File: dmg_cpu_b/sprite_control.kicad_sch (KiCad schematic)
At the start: 138 parts

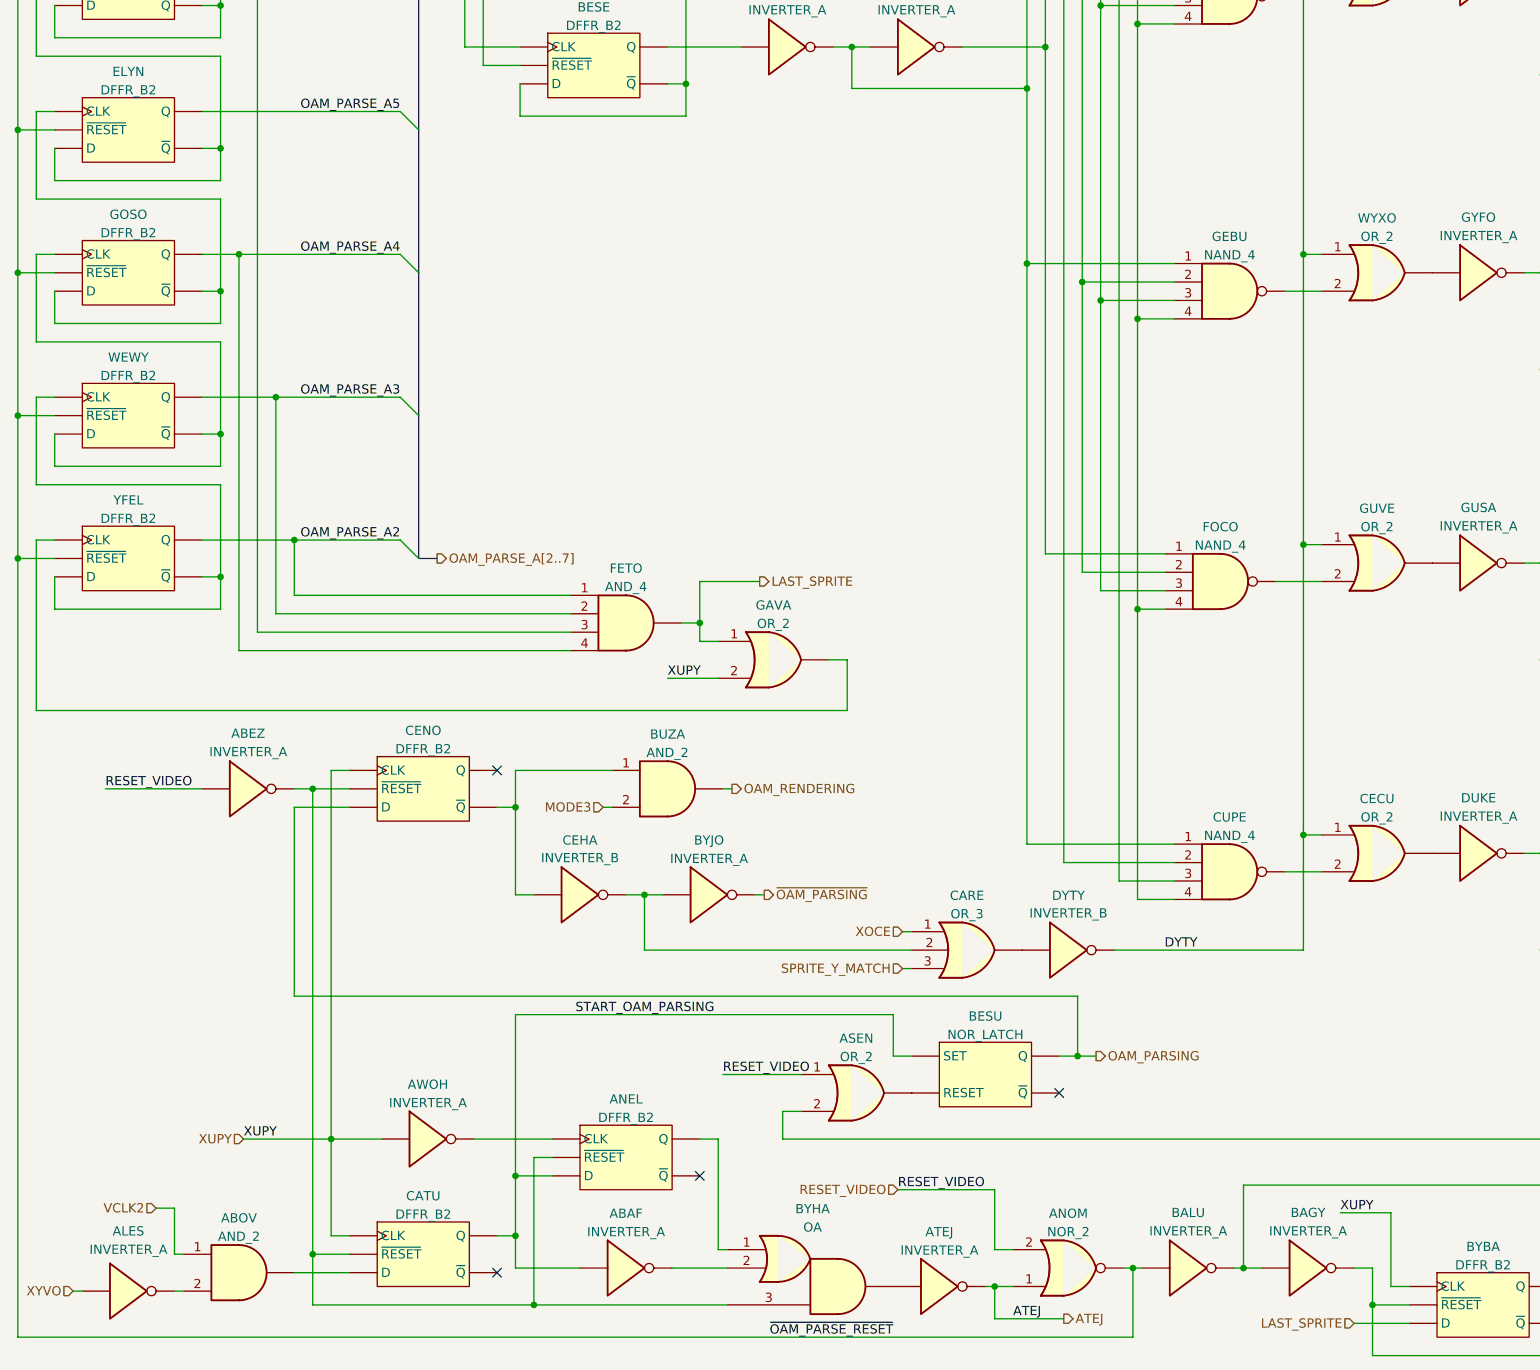
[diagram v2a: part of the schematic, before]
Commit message: Changes made based on review. PPU hierarchcal sheet work started.
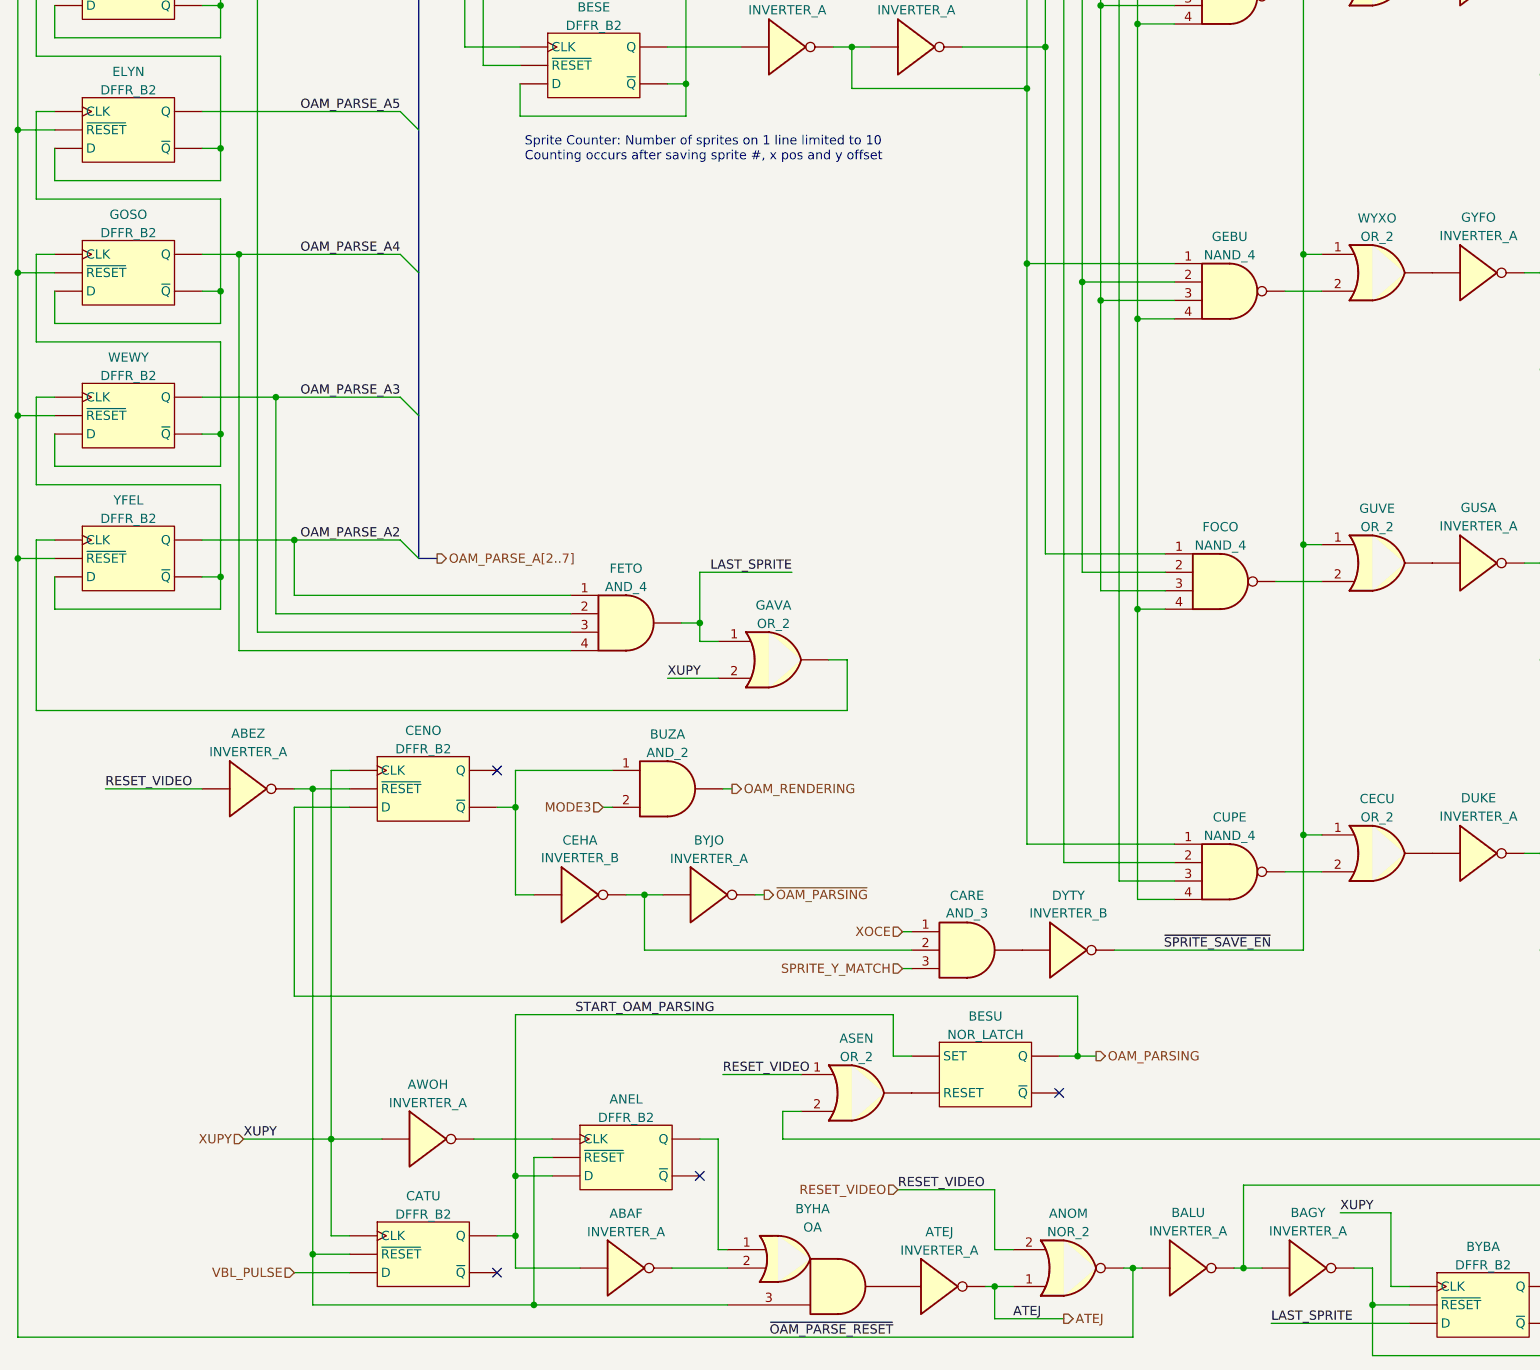
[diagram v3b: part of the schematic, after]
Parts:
- removed ABOV: AND_2, symbol DMG_CPU_Cells:AND_2
- removed ALES: INVERTER_A, symbol DMG_CPU_Cells:INVERTER_A
- CARE: value OR_3 -> AND_3; symbol DMG_CPU_Cells:OR_3 -> DMG_CPU_Cells:AND_3
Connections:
- net VBL_PULSE: now reaches CATU.3 (D)
- net DYTY renamed ~{SPRITE_SAVE_EN}
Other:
- note added: "Sprite Counter: Number of sprites on 1 line limited to 10 Counting occurs after saving sprite #, x pos and y offset"
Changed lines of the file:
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@@
     (stroke (width 0) (type default) (color 0 0 0 0))
   )
-  (wire (pts (xy 24.13 273.685) (xy 25.4 273.685))
-    (stroke (width 0) (type default) (color 0 0 0 0))
-  )
   (wire (pts (xy 46.99 130.81) (xy 46.99 185.42))
     (stroke (width 0) (type default) (color 0 0 0 0))
@@
     (stroke (width 0) (type default) (color 0 0 0 0))
   )
-  (wire (pts (xy 110.49 175.895) (xy 118.745 175.895))
+  (wire (pts (xy 110.49 174.625) (xy 123.19 174.625))
     (stroke (width 0) (type default) (color 0 0 0 0))
   )
@@
     (stroke (width 0) (type default) (color 0 0 0 0))
   )
-  (wire (pts (xy 38.1 262.255) (xy 38.1 268.605))
-    (stroke (width 0) (type default) (color 0 0 0 0))
-  )
   (bus (pts (xy 279.4 135.89) (xy 279.4 95.25))
     (stroke (width 0) (type default) (color 0 0 0 0))
@@
     (stroke (width 0) (type default) (color 0 0 0 0))
   )
-  (wire (pts (xy 110.49 181.61) (xy 110.49 175.895))
+  (wire (pts (xy 110.49 181.61) (xy 110.49 174.625))
     (stroke (width 0) (type default) (color 0 0 0 0))
   )
@@
     (stroke (width 0) (type default) (color 0 0 0 0))
   )
-  (wire (pts (xy 38.1 268.605) (xy 39.37 268.605))
-    (stroke (width 0) (type default) (color 0 0 0 0))
-  )
   (wire (pts (xy 155.575 51.435) (xy 175.895 51.435))
     (stroke (width 0) (type default) (color 0 0 0 0))
@@
     (stroke (width 0) (type default) (color 0 0 0 0))
   )
-  (wire (pts (xy 38.1 273.685) (xy 39.37 273.685))
-    (stroke (width 0) (type default) (color 0 0 0 0))
-  )
   (wire (pts (xy 302.26 51.435) (xy 284.48 51.435))
     (stroke (width 0) (type default) (color 0 0 0 0))
@@
     (stroke (width 0) (type default) (color 0 0 0 0))
   )
-  (wire (pts (xy 200.66 278.13) (xy 208.28 278.13))
+  (wire (pts (xy 189.23 278.13) (xy 208.28 278.13))
     (stroke (width 0) (type default) (color 0 0 0 0))
   )
@@
     (stroke (width 0) (type default) (color 0 0 0 0))
   )
-  (wire (pts (xy 35.56 262.255) (xy 38.1 262.255))
-    (stroke (width 0) (type default) (color 0 0 0 0))
-  )
   (wire (pts (xy 160.655 53.975) (xy 175.895 53.975))
     (stroke (width 0) (type default) (color 0 0 0 0))
@@
     (stroke (width 0) (type default) (color 0 0 0 0))
   )
+  (text "Sprite Counter: Number of sprites on 1 line limited to 10\nCounting occurs after saving sprite #, x pos and y offset"
+    (at 86.36 118.11 0)
+    (effects (font (size 1.27 1.27)) (justify left bottom))
+  )
   (label "SAVE_SPRITE_NUM_0" (at 269.24 66.04 180)
     (effects (font (size 1.27 1.27)) (justify right bottom))
@@
     (effects (font (size 1.27 1.27)) (justify right bottom))
   )
+  (label "LAST_SPRITE" (at 189.23 278.13 0)
+    (effects (font (size 1.27 1.27)) (justify left bottom))
+  )
   (label "SAVE_SPRITE_X_0" (at 269.24 52.705 180)
     (effects (font (size 1.27 1.27)) (justify right bottom))
@@
     (effects (font (size 1.27 1.27)) (justify right bottom))
   )
+  (label "LAST_SPRITE" (at 123.19 174.625 180)
+    (effects (font (size 1.27 1.27)) (justify right bottom))
+  )
   (label "SAVE_SPRITE_NUM_3" (at 269.24 186.69 180)
     (effects (font (size 1.27 1.27)) (justify right bottom))
@@
     (effects (font (size 1.27 1.27)) (justify right bottom))
   )
-  (label "DYTY" (at 179.07 226.695 180)
+  (label "~{SPRITE_SAVE_EN}" (at 189.23 226.695 180)
     (effects (font (size 1.27 1.27)) (justify right bottom))
   )
@@
     (effects (font (size 1.27 1.27)) (justify right bottom))
   )
-  (hierarchical_label "LAST_SPRITE" (shape output) (at 118.745 175.895 0)
-    (effects (font (size 1.27 1.27)) (justify left))
-  )
-  (hierarchical_label "RESET_VIDEO" (shape input) (at 137.795 259.715 180)
+  (hierarchical_label "VBL_PULSE" (shape input) (at 54.61 271.145 180)
     (effects (font (size 1.27 1.27)) (justify right))
   )
-  (hierarchical_label "VCLK2" (shape input) (at 35.56 262.255 180)
+  (hierarchical_label "RESET_VIDEO" (shape input) (at 137.795 259.715 180)
     (effects (font (size 1.27 1.27)) (justify right))
   )
@@
     (effects (font (size 1.27 1.27)) (justify left))
   )
-  (hierarchical_label "XYVO" (shape input) (at 24.13 273.685 180)
-    (effects (font (size 1.27 1.27)) (justify right))
-  )
   (hierarchical_label "OAM_PARSE_A[2..7]" (shape output) (at 74.295 172.72 0)
     (effects (font (size 1.27 1.27)) (justify left))
   )
-  (hierarchical_label "LAST_SPRITE" (shape input) (at 200.66 278.13 180)
-    (effects (font (size 1.27 1.27)) (justify right))
-  )
   (hierarchical_label "MODE3" (shape input) (at 97.155 207.01 180)
     (effects (font (size 1.27 1.27)) (justify right))
@@
     (pin "3")
   )
-  (symbol (lib_id "DMG_CPU_Cells:OR_3") (at 147.32 226.695 0) (unit 1)
-    (in_bom yes) (on_board yes) (fields_autoplaced)
+  (symbol (lib_id "DMG_CPU_Cells:AND_3") (at 147.32 226.695 0) (unit 1)
+    (in_bom yes) (on_board yes)
     (property "Reference" "CARE" (id 0) (at 147.3198 219.1852 0))
-    (property "Value" "OR_3" (id 1) (at 147.3198 221.7221 0))
-    (property "Footprint" "" (id 2) (at 147.066 226.695 0)
+    (property "Value" "AND_3" (id 1) (at 147.32 221.615 0))
+    (property "Footprint" "" (id 2) (at 147.32 226.695 0)
       (effects (font (size 1.27 1.27)) hide)
     )
-    (property "Datasheet" "http://iceboy.a-singer.de/doc/dmg_cells.html#or3" (id 3) (at 147.32 234.315 0)
+    (property "Datasheet" "http://iceboy.a-singer.de/doc/dmg_cells.html#and3" (id 3) (at 147.32 234.315 0)
       (effects (font (size 1.27 1.27)) hide)
     )
@@
     (pin "6")
   )
-  (symbol (lib_id "DMG_CPU_Cells:INVERTER_A") (at 31.75 273.685 0) (unit 1)
-    (in_bom yes) (on_board yes)
-    (property "Reference" "ALES" (id 0) (at 31.75 265.43 0))
-    (property "Value" "INVERTER_A" (id 1) (at 31.75 267.9669 0))
-    (property "Footprint" "" (id 2) (at 29.21 273.685 0)
-      (effects (font (size 1.27 1.27)) hide)
-    )
-    (property "Datasheet" "http://iceboy.a-singer.de/doc/dmg_cells.html#inv_a" (id 3) (at 33.02 281.305 0)
-      (effects (font (size 1.27 1.27)) hide)
-    )
-    (pin "1")
-    (pin "2")
-  )
   (symbol (lib_id "DMG_CPU_Cells:INVERTER_A") (at 233.045 213.36 0) (unit 1)
     (in_bom yes) (on_board yes)
@@
     (pin "2")
   )
-  (symbol (lib_id "DMG_CPU_Cells:AND_2") (at 46.99 271.145 0) (unit 1)
-    (in_bom yes) (on_board yes) (fields_autoplaced)
-    (property "Reference" "ABOV" (id 0) (at 46.99 263.6352 0))
-    (property "Value" "AND_2" (id 1) (at 46.99 266.1721 0))
-    (property "Footprint" "" (id 2) (at 46.99 271.145 0)
-      (effects (font (size 1.27 1.27)) hide)
-    )
-    (property "Datasheet" "http://iceboy.a-singer.de/doc/dmg_cells.html#and2" (id 3) (at 46.99 278.765 0)
-      (effects (font (size 1.27 1.27)) hide)
-    )
-    (pin "1")
-    (pin "2")
-    (pin "3")
-  )
   (symbol (lib_id "DMG_CPU_Cells:INVERTER_A") (at 217.805 173.355 0) (unit 1)
